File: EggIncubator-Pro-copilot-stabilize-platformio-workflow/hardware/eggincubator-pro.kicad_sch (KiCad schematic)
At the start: 8 parts, among them J1 ESP32 DevKit breakout, J2 SHT31 module, I2C 0x44, J3 DS18B20, 1-Wire, J4 4-channel relay / SSR inputs, J5 BTS7960 module / motor, J6 Door and turner limit switches, J7 Buzzer module

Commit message: Link KiCad design from README
Co-authored-by: tomnyle <175001228+tomnyle@users.noreply.github.com>
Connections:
- net BUZZER: now also J7.1
- net GND: now also J7.2
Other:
- note added: "J1 pin map continued: 10=GPIO32/RPWM, 11=GPIO33/LPWM, 12=GPIO23/R_EN+L_EN, 13=GPIO18/HOME, 14=GPIO19/END, 15=GPIO13/door, 16=GPIO4/buzzer, 17=GPIO2/optional status LED."
- note added: "Matching local labels connect nets. J1 pin map: 1=3V3, 2=GND, 3=GPIO21/SDA, 4=GPIO22/SCL, 5=GPIO17/DS18B20_DQ, 6=GPIO25/heater, 7=GPIO26/humidifier, 8=GPIO27/circulation fan, 9=GPIO14/ventilation fan."
- note added: "Relay controls are active LOW. J6 dry contacts connect each named signal to GND; firmware configures INPUT_PULLUP."
- note removed: "GPIO labels with identical names are electrically connected by KiCad global-label net matching."
- note removed: "J1 ESP32: pin breakout follows include/pins.h. GPIO23 drives both BTS7960 enable inputs. Relay controls are active LOW."
- note removed: "J6 switches: connect each dry contact between its named signal and GND; firmware configures INPUT_PULLUP."
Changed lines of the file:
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@@
   (label "3V3" (at 185 154.19 90) (fields_autoplaced yes) (effects (font (size 1.27 1.27)) (justify left bottom)))
   (label "ONEWIRE_DQ" (at 185 161.81 270) (fields_autoplaced yes) (effects (font (size 1.27 1.27)) (justify left bottom)))
-  (text "GPIO labels with identical names are electrically connected by KiCad global-label net matching." (at 45 205 0) (effects (font (size 1.5 1.5))))
-  (text "J1 ESP32: pin breakout follows include/pins.h. GPIO23 drives both BTS7960 enable inputs. Relay controls are active LOW." (at 45 215 0) (effects (font (size 1.5 1.5))))
-  (text "J6 switches: connect each dry contact between its named signal and GND; firmware configures INPUT_PULLUP." (at 45 225 0) (effects (font (size 1.5 1.5))))
+  (text "Matching local labels connect nets. J1 pin map: 1=3V3, 2=GND, 3=GPIO21/SDA, 4=GPIO22/SCL, 5=GPIO17/DS18B20_DQ, 6=GPIO25/heater, 7=GPIO26/humidifier, 8=GPIO27/circulation fan, 9=GPIO14/ventilation fan." (at 45 205 0) (effects (font (size 1.5 1.5))))
+  (text "J1 pin map continued: 10=GPIO32/RPWM, 11=GPIO33/LPWM, 12=GPIO23/R_EN+L_EN, 13=GPIO18/HOME, 14=GPIO19/END, 15=GPIO13/door, 16=GPIO4/buzzer, 17=GPIO2/optional status LED." (at 45 215 0) (effects (font (size 1.5 1.5))))
+  (text "Relay controls are active LOW. J6 dry contacts connect each named signal to GND; firmware configures INPUT_PULLUP." (at 45 225 0) (effects (font (size 1.5 1.5))))
   (text "R1 is the recommended 4.7 kOhm DS18B20 pull-up between 3V3 and ONEWIRE_DQ. SHT31 SDA/SCL are separate." (at 45 235 0) (effects (font (size 1.5 1.5))))
   (text "Use 3.3 V-compatible relay/SSR inputs. Relay/driver logic supply voltage and load-side wiring depend on the exact module." (at 45 245 0) (effects (font (size 1.5 1.5))))

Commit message: Validate and refine KiCad schematic
Co-authored-by: tomnyle <175001228+tomnyle@users.noreply.github.com>
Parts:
- J1: symbol EggIncubator:Header_01x17 -> Connector_Generic:Conn_01x17
- J2: symbol EggIncubator:Header_01x04 -> Connector_Generic:Conn_01x04
- J3: symbol EggIncubator:Header_01x03 -> Connector_Generic:Conn_01x03
- J4, J6: symbol EggIncubator:Header_01x06 -> Connector_Generic:Conn_01x06
- J5: symbol EggIncubator:Header_01x09 -> Connector_Generic:Conn_01x10
- J7: symbol EggIncubator:Header_01x02 -> Connector_Generic:Conn_01x02
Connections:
- net MOTOR_B: now also J5.10
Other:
- note added: "J1 pins 10-17: GPIO32/RPWM, GPIO33/LPWM, GPIO23/R_EN+L_EN, GPIO18/HOME, GPIO19/END, GPIO13/door, GPIO4/buzzer, GPIO2/optional status LED."
- note added: "Local labels with identical names connect nets. J1 pins 1-9: 3V3, GND, GPIO21/SDA, GPIO22/SCL, GPIO17/DS18B20, GPIO25/heater, GPIO26/humidifier, GPIO27/circulation fan, GPIO14/ventilation fan."
- note added: "Mains/heater/load wiring is omitted. Use correctly rated isolation, fusing, enclosures, and qualified mains installation."
- note added: "R1 is the recommended 4.7 kOhm DS18B20 pull-up between 3V3 and ONEWIRE_DQ. SHT31 SDA/SCL remain separate."
- note added: "Use 3.3 V-compatible relay/SSR inputs. Module logic supply and load wiring depend on the selected module."
- note added: "Use a separate DC motor supply per BTS7960/motor ratings; connect logic grounds per the driver datasheet."
- note removed: "J1 pin map continued: 10=GPIO32/RPWM, 11=GPIO33/LPWM, 12=GPIO23/R_EN+L_EN, 13=GPIO18/HOME, 14=GPIO19/END, 15=GPIO13/door, 16=GPIO4/buzzer, 17=GPIO2/optional status LED."
- note removed: "Mains/heater/load wiring is intentionally omitted. Use correctly rated isolation, fusing and qualified mains installation."
- note removed: "Matching local labels connect nets. J1 pin map: 1=3V3, 2=GND, 3=GPIO21/SDA, 4=GPIO22/SCL, 5=GPIO17/DS18B20_DQ, 6=GPIO25/heater, 7=GPIO26/humidifier, 8=GPIO27/circulation fan, 9=GPIO14/ventilation fan."
- note removed: "R1 is the recommended 4.7 kOhm DS18B20 pull-up between 3V3 and ONEWIRE_DQ. SHT31 SDA/SCL are separate."
- note removed: "Use 3.3 V-compatible relay/SSR inputs. Relay/driver logic supply voltage and load-side wiring depend on the exact module."
- note removed: "Use a separate DC motor supply per BTS7960/motor ratings; connect logic grounds as specified by the module datasheet."
- moved on the sheet: R1

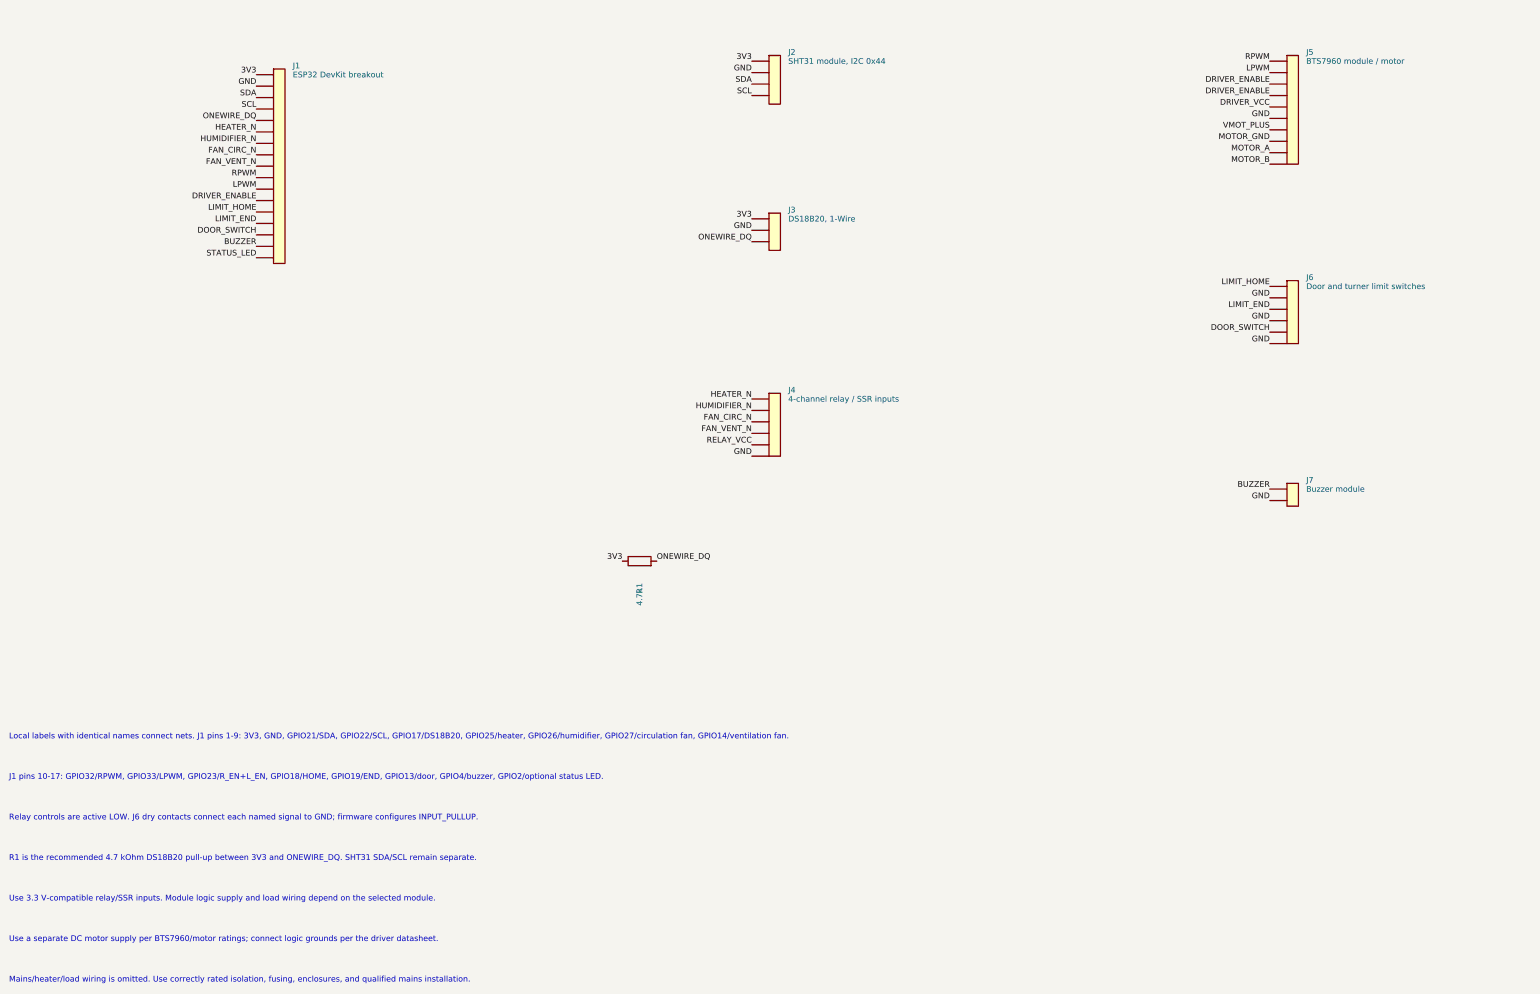
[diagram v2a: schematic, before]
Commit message: Complete modular KiCad control schematic
Co-authored-by: tomnyle <175001228+tomnyle@users.noreply.github.com>
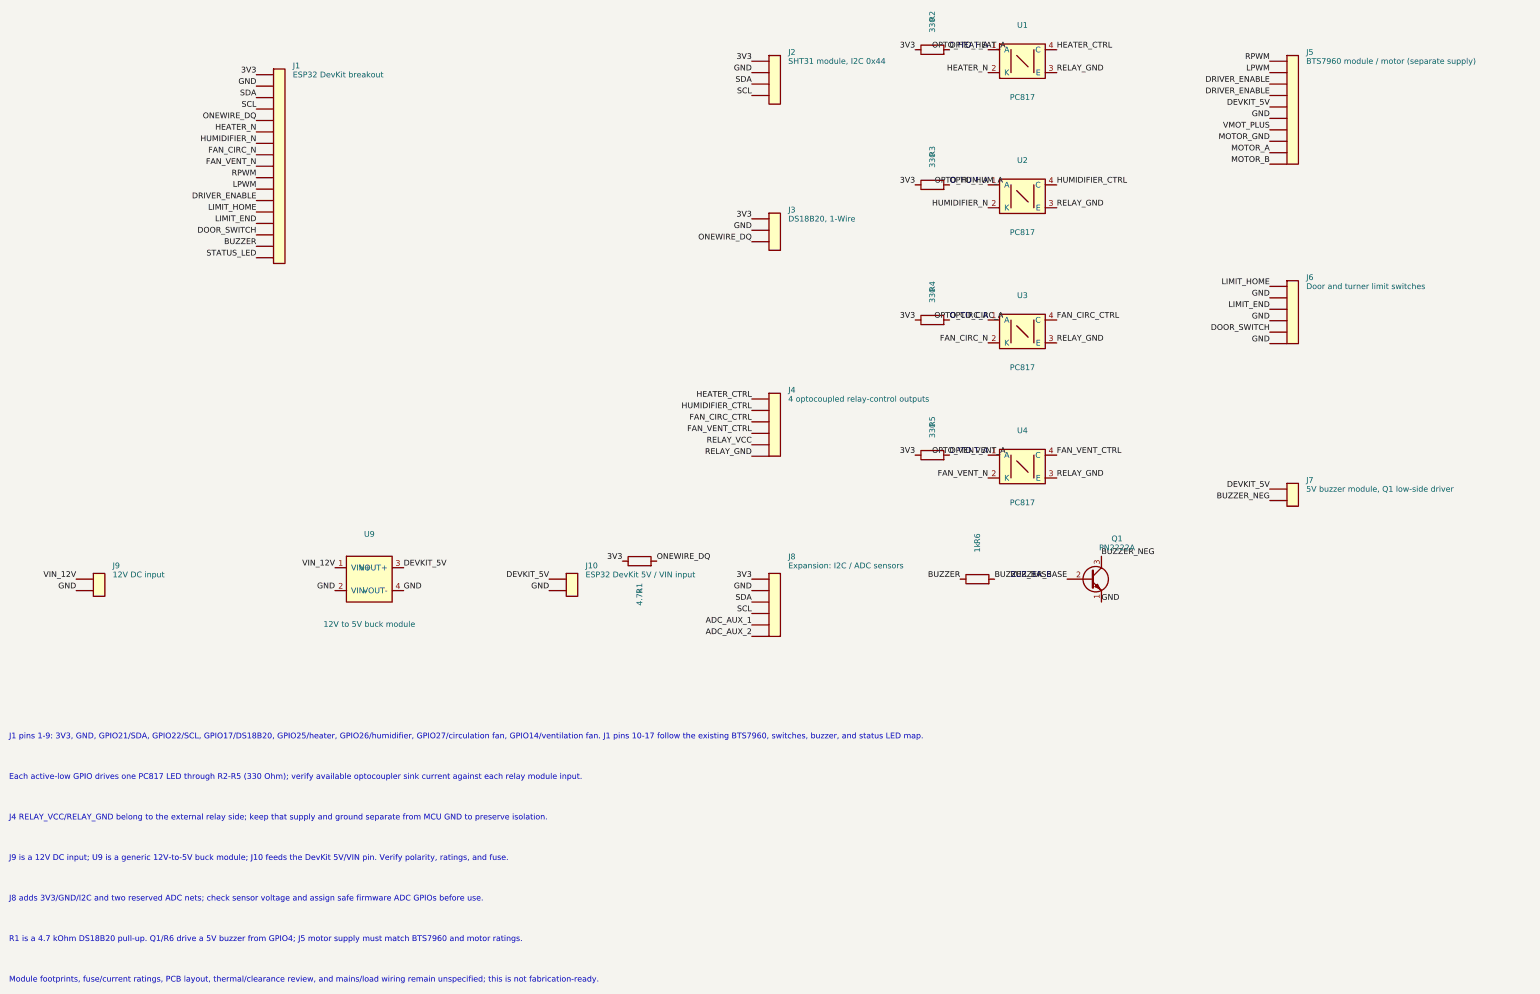
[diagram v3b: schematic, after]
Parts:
- added J10: ESP32 DevKit 5V / VIN input, symbol Connector_Generic:Conn_01x02
- added J8: Expansion: I2C / ADC sensors, symbol Connector_Generic:Conn_01x06
- added J9: 12V DC input, symbol Connector_Generic:Conn_01x02
- added Q1: PN2222A, Package_TO_SOT_THT:TO-92_Inline, symbol Transistor_BJT:PN2222A
- added R2, R3, R4, R5: 330, symbol Device:R
- added R6: 1k, symbol Device:R
- added U1, U2, U3, U4: PC817, Package_DIP:DIP-4_W7.62mm, symbol Isolator:PC817
- added U9: 12V to 5V buck module, symbol EggIncubator:DC_DC_Module
- J4: value 4-channel relay / SSR inputs -> 4 optocoupled relay-control outputs
- J5: value BTS7960 module / motor -> BTS7960 module / motor (separate supply)
- J7: value Buzzer module -> 5V buzzer module, Q1 low-side driver
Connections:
- net 3V3: now also J8.1, R2.1, R3.1, R4.1, R5.1
- net BUZZER: now also R6.1; no longer J7.1
- net FAN_CIRC_N: now also U3.2 (K); no longer J4.3
- net FAN_VENT_N: now also U4.2 (K); no longer J4.4
- net GND: now also J10.2, J8.2, J9.2, Q1.1 (E), U9.2 (VIN-), U9.4 (VOUT-); no longer J4.6, J7.2
- net HEATER_N: now also U1.2 (K); no longer J4.1
- net HUMIDIFIER_N: now also U2.2 (K); no longer J4.2
- net SCL: now also J8.4
- net SDA: now also J8.3
- net DRIVER_VCC renamed DEVKIT_5V
- net DEVKIT_5V: now also J7.1, J10.1, U9.3 (VOUT+)
- new net ADC_AUX_1: J8.5
- new net ADC_AUX_2: J8.6
- new net BUZZER_BASE: Q1.2 (B), R6.2
- new net BUZZER_NEG: J7.2, Q1.3 (C)
- new net FAN_CIRC_CTRL: J4.3, U3.4 (C)
- new net FAN_VENT_CTRL: J4.4, U4.4 (C)
- new net HEATER_CTRL: J4.1, U1.4 (C)
- new net HUMIDIFIER_CTRL: J4.2, U2.4 (C)
- new net OPTO_CIRC_A: R4.2, U3.1 (A)
- new net OPTO_HEAT_A: R2.2, U1.1 (A)
- new net OPTO_HUM_A: R3.2, U2.1 (A)
- new net OPTO_VENT_A: R5.2, U4.1 (A)
- new net RELAY_GND: J4.6, U1.3 (E), U2.3 (E), U3.3 (E), U4.3 (E)
- new net VIN_12V: J9.1, U9.1 (VIN+)
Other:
- note added: "Each active-low GPIO drives one PC817 LED through R2-R5 (330 Ohm); verify available optocoupler sink current against each relay module input."
- note added: "J1 pins 1-9: 3V3, GND, GPIO21/SDA, GPIO22/SCL, GPIO17/DS18B20, GPIO25/heater, GPIO26/humidifier, GPIO27/circulation fan, GPIO14/ventilation fan. J1 pins 10-17 follow the existing BTS7960, switches, buzzer, and status LED map."
- note added: "J4 RELAY_VCC/RELAY_GND belong to the external relay side; keep that supply and ground separate from MCU GND to preserve isolation."
- note added: "J8 adds 3V3/GND/I2C and two reserved ADC nets; check sensor voltage and assign safe firmware ADC GPIOs before use."
- note added: "J9 is a 12V DC input; U9 is a generic 12V-to-5V buck module; J10 feeds the DevKit 5V/VIN pin. Verify polarity, ratings, and fuse."
- note added: "Module footprints, fuse/current ratings, PCB layout, thermal/clearance review, and mains/load wiring remain unspecified; this is not fabrication-ready."
- note added: "R1 is a 4.7 kOhm DS18B20 pull-up. Q1/R6 drive a 5V buzzer from GPIO4; J5 motor supply must match BTS7960 and motor ratings."
- note removed: "J1 pins 10-17: GPIO32/RPWM, GPIO33/LPWM, GPIO23/R_EN+L_EN, GPIO18/HOME, GPIO19/END, GPIO13/door, GPIO4/buzzer, GPIO2/optional status LED."
- note removed: "Local labels with identical names connect nets. J1 pins 1-9: 3V3, GND, GPIO21/SDA, GPIO22/SCL, GPIO17/DS18B20, GPIO25/heater, GPIO26/humidifier, GPIO27/circulation fan, GPIO14/ventilation fan."
- note removed: "Mains/heater/load wiring is omitted. Use correctly rated isolation, fusing, enclosures, and qualified mains installation."
- note removed: "R1 is the recommended 4.7 kOhm DS18B20 pull-up between 3V3 and ONEWIRE_DQ. SHT31 SDA/SCL remain separate."
- note removed: "Relay controls are active LOW. J6 dry contacts connect each named signal to GND; firmware configures INPUT_PULLUP."
- note removed: "Use 3.3 V-compatible relay/SSR inputs. Module logic supply and load wiring depend on the selected module."
- note removed: "Use a separate DC motor supply per BTS7960/motor ratings; connect logic grounds per the driver datasheet."

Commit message: Complete schematic circuit details
Co-authored-by: tomnyle <175001228+tomnyle@users.noreply.github.com>
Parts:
- added C1: 470uF 25V, symbol EggIncubator:CP
- added C2: 470uF 10V, symbol EggIncubator:CP
- added D1: Status LED, symbol EggIncubator:LED
- added F1: Fuse (rate per load), symbol EggIncubator:Fuse
- added R10, R7, R8, R9: 4.7k, symbol Device:R
- added R11, R12: 4.7k optional, symbol Device:R
- added R13: 1k, symbol Device:R
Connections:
- net MOTOR_GND is gone; now on net GND: J5.8
- net 3V3: now also R11.1, R12.1
- net DEVKIT_5V: now also C2.1 (+)
- net FAN_CIRC_CTRL: now also R9.2
- net FAN_VENT_CTRL: now also R10.2
- net GND: now also C1.2 (-), C2.2 (-), D1.2 (K)
- net HEATER_CTRL: now also R7.2
- net HUMIDIFIER_CTRL: now also R8.2
- net RELAY_VCC: now also R10.1, R7.1, R8.1, R9.1
- net SCL: now also R12.2
- net SDA: now also R11.2
- net STATUS_LED: now also R13.1
- net VIN_12V: now also C1.1 (+), F1.2; no longer J9.1
- new net LED_ANODE: D1.1 (A), R13.2
- new net RAW_12V: F1.1, J9.1
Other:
- note added: "Each active-low GPIO drives one PC817 LED through R2-R5 (330 Ohm); R7-R10 pull CTRL up to isolated RELAY_VCC. Verify opto sink current."
- note added: "J9 is a 12V DC input; F1 is in series; C1/C2 are bulk capacitors. U9 is a generic 12V-to-5V buck; J10 feeds DevKit 5V/VIN."
- note added: "R1 is the DS18B20 pull-up; R13/D1 provide a GPIO2 status LED. Q1/R6 drive the 5V buzzer; J5 BTS7960 motor and logic returns are common."
- note added: "R11/R12 are optional I2C pull-ups; leave DNP if the sensor breakout already includes them. J8 ADC nets are reserved for firmware assignment."
- note removed: "Each active-low GPIO drives one PC817 LED through R2-R5 (330 Ohm); verify available optocoupler sink current against each relay module input."
- note removed: "J8 adds 3V3/GND/I2C and two reserved ADC nets; check sensor voltage and assign safe firmware ADC GPIOs before use."
- note removed: "J9 is a 12V DC input; U9 is a generic 12V-to-5V buck module; J10 feeds the DevKit 5V/VIN pin. Verify polarity, ratings, and fuse."
- note removed: "R1 is a 4.7 kOhm DS18B20 pull-up. Q1/R6 drive a 5V buzzer from GPIO4; J5 motor supply must match BTS7960 and motor ratings."
